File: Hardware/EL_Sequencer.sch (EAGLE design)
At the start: 109 parts, among them J1 Battery, J2 DC-OUTPUT, J3 AC-INPUT, U1 LM317, U10 Z0103MN, U11 Z0103MN, U12 Z0103MN, U13 MOC3063S, U14 MOC3063S, U15 MOC3063S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

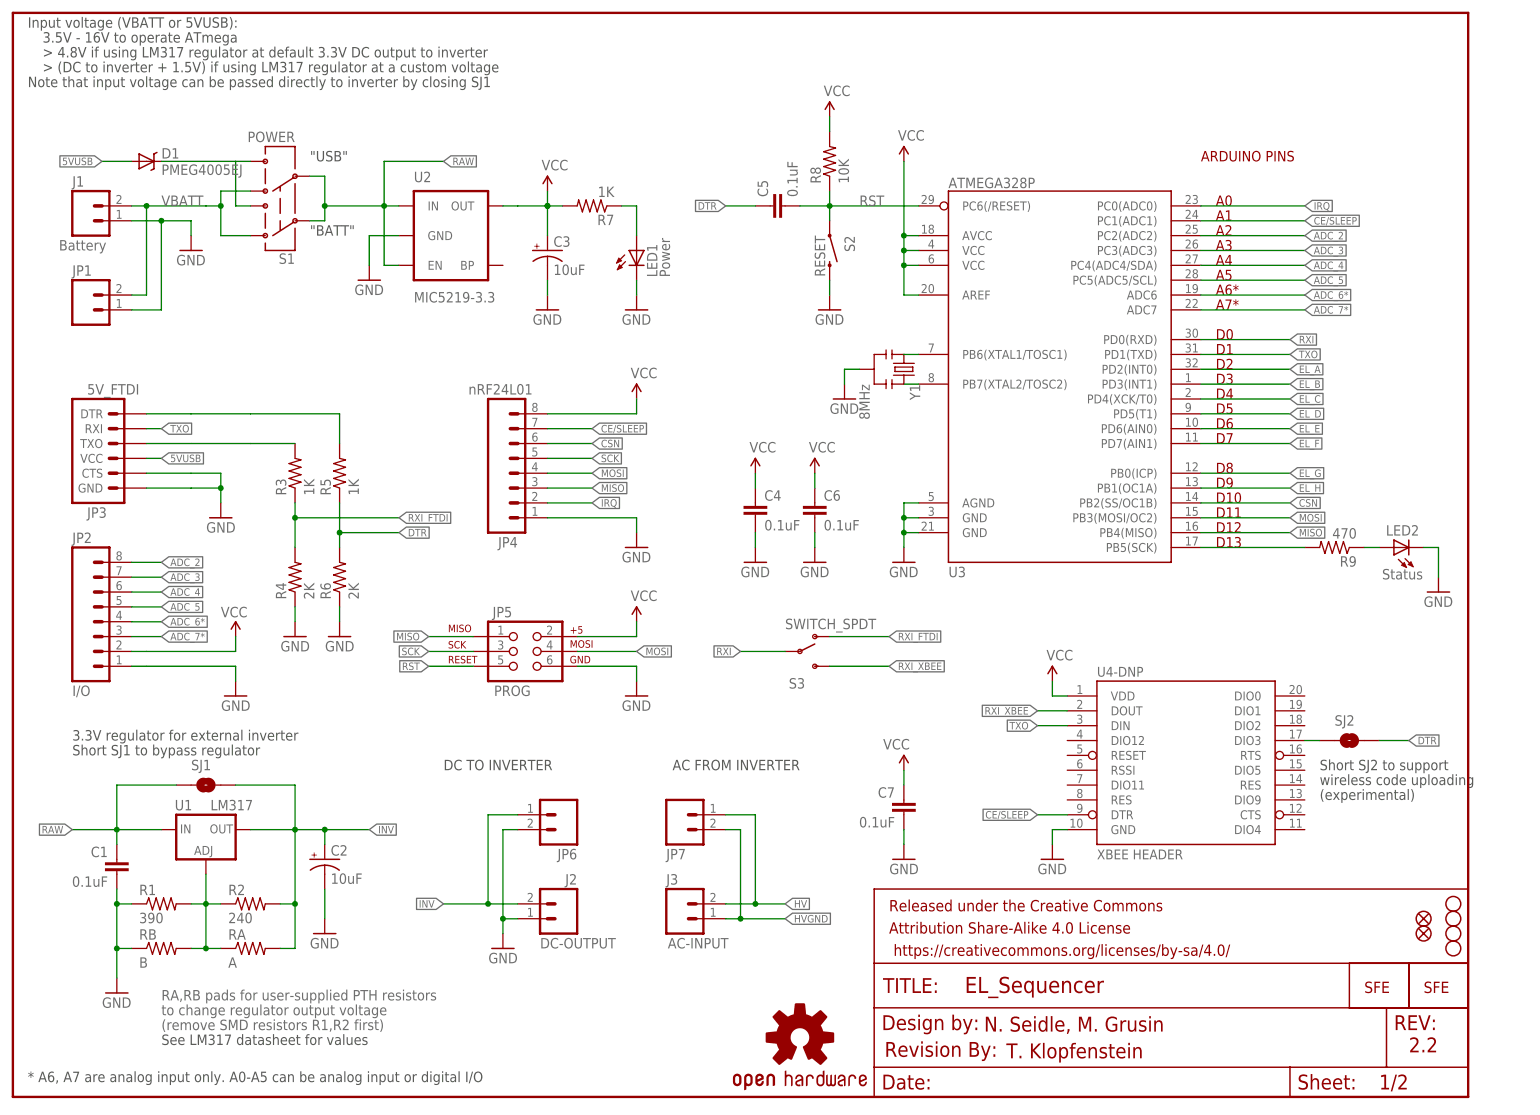
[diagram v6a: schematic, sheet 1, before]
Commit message: Updates to V2.3
> Swapped LED resistors LED1 (green) now has 470, LED2 (red) now has 1K
> Added heatsink pours for 3.3V reg U2
> Reworked FTDI/XBEE switch, throw is now in direction of respective
connectors, swapped silk, added silk to bottom
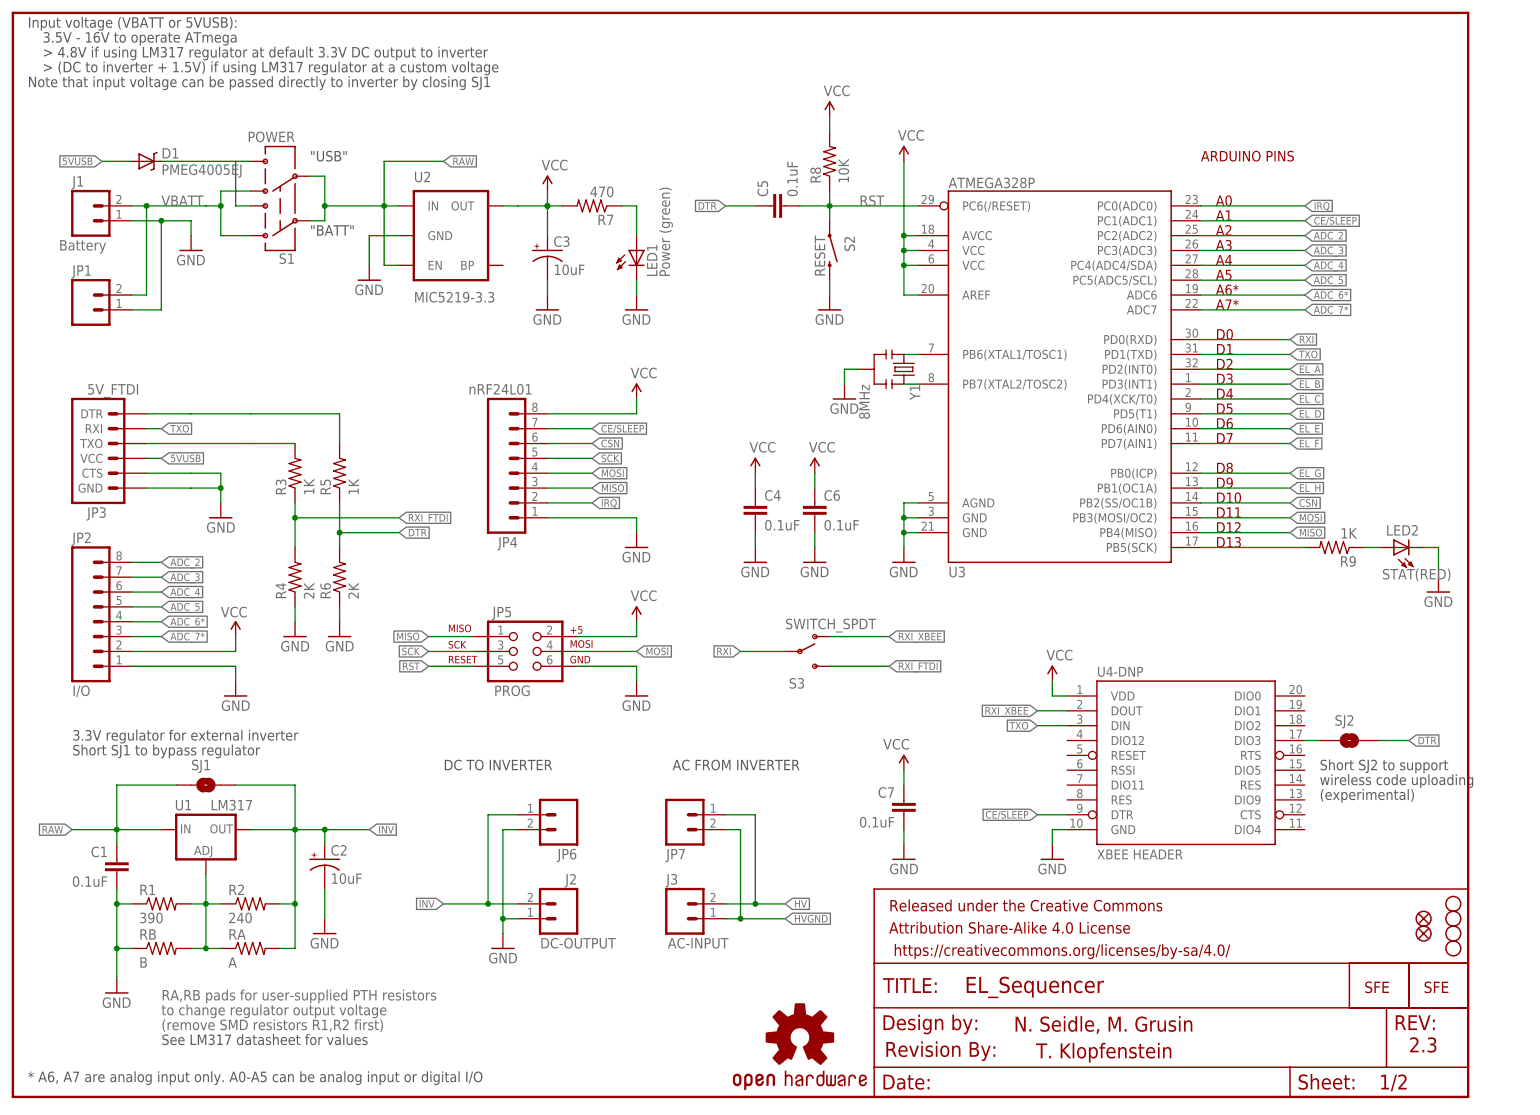
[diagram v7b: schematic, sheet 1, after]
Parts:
- LED1: value Power -> Power (green)
- LED2: value Status -> STAT(RED)
- R7: value 1K -> 470
- R9: value 470 -> 1K
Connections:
- net RXI_FTDI: now also S3.S; no longer S3.O
- net RXI_XBEE: now also S3.O; no longer S3.S
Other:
- note added: "2.3"
- note removed: "2.2"
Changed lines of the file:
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@@
 <part name="C6" library="SparkFun-Capacitors" deviceset="0.1UF-25V(+80/-20%)(0603)" device="" value="0.1uF"/>
 <part name="GND11" library="supply1" deviceset="GND" device=""/>
-<part name="R7" library="SparkFun-Resistors" deviceset="1KOHM1/10W1%(0603)" device="" value="1K"/>
-<part name="LED1" library="SparkFun" deviceset="LED" device="0603" value="Power"/>
+<part name="R7" library="SparkFun-Resistors" deviceset="1KOHM1/10W1%(0603)" device="" value="470"/>
+<part name="LED1" library="SparkFun" deviceset="LED" device="0603" value="Power (green)"/>
 <part name="GND9" library="SparkFun" deviceset="GND" device=""/>
 <part name="C3" library="SparkFun-Capacitors" deviceset="10UF-16V-10%(TANT)" device="" value="10uF"/>
@@
 <part name="U$5" library="SparkFun" deviceset="STAND-OFF" device=""/>
 <part name="U3" library="SparkFun" deviceset="ATMEGA168" device="" value="ATMEGA328P"/>
-<part name="LED2" library="SparkFun" deviceset="LED" device="0603" value="Status"/>
-<part name="R9" library="SparkFun-Resistors" deviceset="1KOHM1/10W1%(0603)" device="" value="470"/>
+<part name="LED2" library="SparkFun" deviceset="LED" device="0603" value="STAT(RED)"/>
+<part name="R9" library="SparkFun-Resistors" deviceset="1KOHM1/10W1%(0603)" device="" value="1K"/>
 <part name="GND14" library="SparkFun" deviceset="GND" device=""/>
 <part name="GND15" library="SparkFun" deviceset="GND" device=""/>
@@
 <text x="205.74" y="96.52" size="1.778" layer="94">D12</text>
 <text x="205.74" y="93.98" size="1.778" layer="94">D13</text>
-<text x="166.116" y="11.176" size="2.54" layer="94">N. Seidle, M. Grusin</text>
-<text x="238.76" y="7.62" size="2.54" layer="94">2.2</text>
+<text x="171.196" y="11.176" size="2.54" layer="94">N. Seidle, M. Grusin</text>
+<text x="238.76" y="7.62" size="2.54" layer="94">2.3</text>
 <text x="10.16" y="58.42" size="1.778" layer="97">Short SJ1 to bypass regulator</text>
 <text x="10.16" y="60.96" size="1.778" layer="97">3.3V regulator for external inverter</text>
@@
 <text x="50.8" y="160.02" size="1.778" layer="97">"USB"</text>
 <text x="50.8" y="147.32" size="1.778" layer="97">"BATT"</text>
-<text x="169.926" y="6.604" size="2.54" layer="94">T. Klopfenstein</text>
+<text x="175.006" y="6.604" size="2.54" layer="94">T. Klopfenstein</text>
 </plain>
 <instances>
@@
 <net name="RXI_FTDI" class="0">
 <segment>
-<pinref part="S3" gate="G$1" pin="O"/>
-<wire x1="139.7" y1="78.74" x2="149.86" y2="78.74" width="0.2032" layer="91"/>
-<label x="149.86" y="78.74" size="1.27" layer="95" xref="yes"/>
+<label x="149.86" y="73.66" size="1.27" layer="95" xref="yes"/>
+<wire x1="139.7" y1="73.66" x2="149.86" y2="73.66" width="0.2032" layer="91"/>
+<pinref part="S3" gate="G$1" pin="S"/>
 </segment>
 <segment>
@@
 <net name="RXI_XBEE" class="0">
 <segment>
-<pinref part="S3" gate="G$1" pin="S"/>
-<wire x1="139.7" y1="73.66" x2="149.86" y2="73.66" width="0.2032" layer="91"/>
-<label x="149.86" y="73.66" size="1.27" layer="95" xref="yes"/>
-</segment>
-<segment>
+<label x="149.86" y="78.74" size="1.27" layer="95" xref="yes"/>
+<wire x1="139.7" y1="78.74" x2="149.86" y2="78.74" width="0.2032" layer="91"/>
+<pinref part="S3" gate="G$1" pin="O"/>
+</segment>
+<segment>

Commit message: Updating parts to proper libraries, swapped stat LED to blue
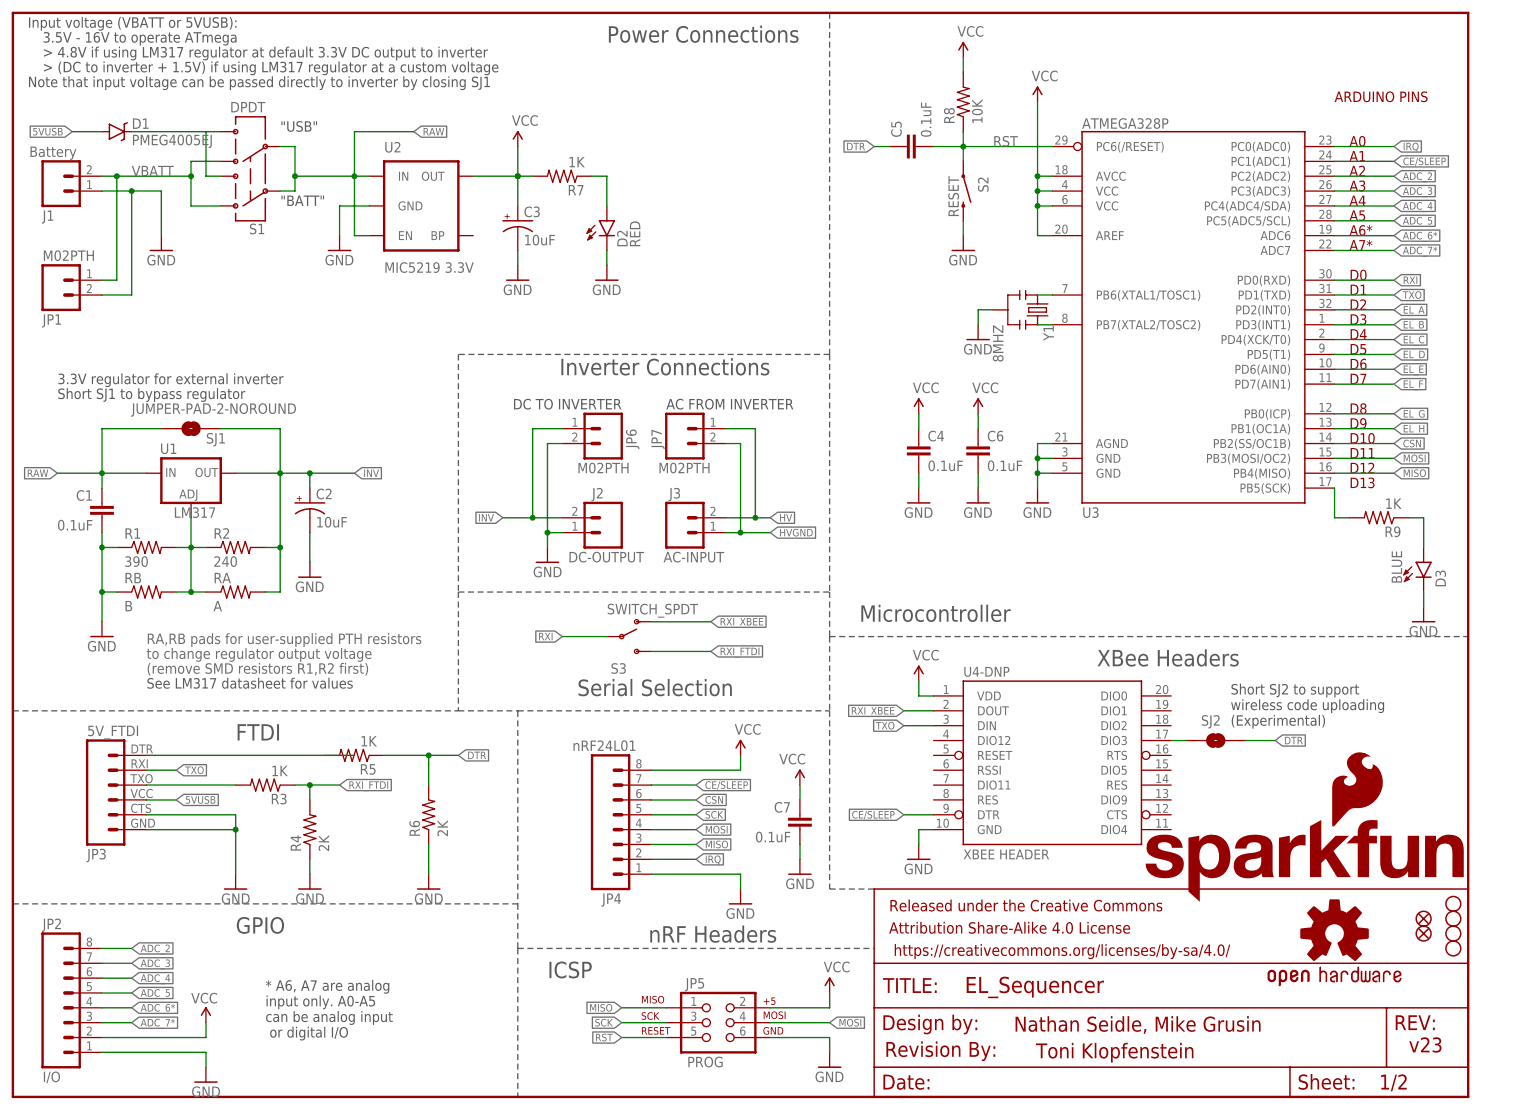
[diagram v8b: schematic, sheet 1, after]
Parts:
- removed LED1: Power (green), SparkFun:LED0603
- removed LED2: STAT(RED), SparkFun:LED0603
- added D2: RED, SparkFun-LED:LED-RED0603
- added D3: BLUE, SparkFun-LED:LED-BLUE0603
- J1, J2, J3: device SparkFun:M02-JST-2MM-SMT -> SparkFun-Connectors:M02-JST-2MM-SMT
- J10, J11, J4, J5, J6, J7, J8, J9: value (none) -> M02-JST-2MM-SMT; device SparkFun:M02-JST-2MM-SMT -> SparkFun-Connectors:M02-JST-2MM-SMT
- JP1, JP10, JP11, JP12, JP13, JP14, JP15, JP16, JP6, JP7, JP9: value (none) -> M02PTH; device SparkFun:M02PTH -> SparkFun-Connectors:M02PTH
- JP2: device mike-temp:M08_ROUND -> SparkFun-Connectors:M08
- JP3: device SparkFun:ARDUINO_SERIAL_PROGRAMPTH -> SparkFun-Connectors:FTDI_BASICPTH
- JP4: device SparkFun:M081X08 -> SparkFun-Connectors:M08SILK_FEMALE_PTH
- JP5: device SparkFun:AVR_SPI_PRG_6PTH -> SparkFun-Connectors:AVR_SPI_PRG_6PTH
- JP8: value LOGO-SFESK -> SFE_LOGO_FLAME.2_INCH; device SparkFun-Aesthetics:LOGO-SFESK -> SparkFun-Aesthetics:SFE_LOGO_FLAME.2_INCH
- R3, R5, R9: device SparkFun-Resistors:1KOHM1/10W1%(0603) -> SparkFun-Resistors:1KOHM-1/10W-1%(0603)
- R7: value 470 -> 1K; device SparkFun-Resistors:1KOHM1/10W1%(0603) -> SparkFun-Resistors:1KOHM-1/10W-1%(0603)
- R8: device SparkFun-Resistors:10KOHM1/10W1%(0603)0603 -> SparkFun-Resistors:10KOHM-1/10W-1%(0603)0603
- RA, RB: device SparkFun:RESISTORPTH-1/4W -> SparkFun-Resistors:RESISTORPTH-1/4W
- S1: value POWER -> DPDT; device SparkFun:SWITCH-DPDTSMD -> SparkFun-Electromechanical:SWITCH-DPDTAYZ0202
- S2: device SparkFun:SWITCH-MOMENTARY-2SMD -> SparkFun-Electromechanical:SWITCH-MOMENTARY-2SMD
- SJ1: value SOLDERJUMPERROUND -> JUMPER-PAD-2-NOROUND; device mike-temp:SOLDERJUMPERROUND -> SparkFun-Passives:JUMPER-PAD-2-NOROUND
- SJ2: value SOLDERJUMPERNO -> JUMPER-PAD-2-NOYES_SILK; device SparkFun-Passives:SOLDERJUMPERNO -> SparkFun-Passives:JUMPER-PAD-2-NOYES_SILK
- U$1: value OSHW-LOGOS -> OSHW-LOGOM; device SparkFun-Aesthetics:OSHW-LOGOS -> SparkFun-Aesthetics:OSHW-LOGOM
- U$2: value LOGO-SFENEW -> SFE_LOGO_NAME_FLAME.2_INCH; device SparkFun:LOGO-SFENEW -> SparkFun-Aesthetics:SFE_LOGO_NAME_FLAME.2_INCH
- U$5, U$6, U$7, U$8: device SparkFun:STAND-OFF -> SparkFun-Electromechanical:STAND-OFF
- U1: device SparkFun:V_REG_317DPACK -> SparkFun-PowerIC:V_REG_317DPACK
- U10, U11, U12, U17, U18, U19, U20, U9: device mike-temp:TRIACSMD -> SparkFun-DiscreteSemi:TRIAC-HPSMD
- U13, U14, U15, U16, U5, U6, U7, U8: device mike-temp:MOC3063S -> SparkFun-DiscreteSemi:MOC3063S
- U2: value MIC5219-3.3 -> MIC5219 3.3V; device SparkFun:V_REG_LDOSMD -> SparkFun-PowerIC:V_REG_MIC52193.3V
- U3: device SparkFun:ATMEGA168 -> SparkFun-DigitalIC:ATMEGA328_SMT
- U4-DNP: device mike-temp:XBEE-1LONGPAD -> SparkFun-RF:XBEE-1LONGPAD
- Y1: value 8MHz -> 8MHZ; device SparkFun:RESONATORSMD -> SparkFun-FreqCtrl:RESONATOR8MHZ
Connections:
- net 5VUSB: now also JP3.4; no longer JP3.VCC
- net FTDI_DTR: now also JP3.1; no longer JP3.DTR
- net FTDI_RXI: now also JP3.3; no longer JP3.TXO
- net GND: now also D2.C, D3.C, J1.2, J2.2, JP1.2, JP3.5, JP3.6; no longer J1.1, J2.1, JP1.1, JP3.CTS, JP3.GND, LED1.C, LED2.C
- net HV: now also J3.1; no longer J3.2
- net HVGND: now also J10.2, J11.2, J3.2, J4.2, J5.2, J6.2, J7.2, J8.2, J9.2; no longer J10.1, J11.1, J3.1, J4.1, J5.1, J6.1, J7.1, J8.1, J9.1
- net INV: now also J2.1; no longer J2.2
- net N$14: now also D3.A; no longer LED2.A
- net N$16: now also J6.1; no longer J6.2
- net N$20: now also J7.1; no longer J7.2
- net N$21: now also J4.1; no longer J4.2
- net N$25: now also J8.1; no longer J8.2
- net N$29: now also J9.1; no longer J9.2
- net N$33: now also J10.1; no longer J10.2
- net N$37: now also J11.1; no longer J11.2
- net N$4: now also D2.A; no longer LED1.A
- net N$9: now also J5.1; no longer J5.2
- net TXO: now also JP3.2; no longer JP3.RXI
- net VBATT: now also J1.1, JP1.1; no longer J1.2, JP1.2
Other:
- note added: "EL Channels"
- note added: "FTDI"
- note added: "GPIO"
- note added: "ICSP"
- note added: "Inverter Connections"
- note added: "Microcontroller"
- note added: "Nathan Seidle, Mike Grusin"
- note added: "Power Connections"
- note added: "Revision by: Toni Klopfenstein"
- note added: "Serial Selection"
- note added: "Short SJ2 to support wireless code uploading (Experimental)"
- note added: "Toni Klopfenstein"
- note added: "XBee Headers"
- note added: "nRF Headers"
- note added: "v23"
- note removed: "(experimental)"
- note removed: "2.1"
- note removed: "2.3"
- note removed: "Short SJ2 to support"
- note removed: "T. Klopfenstein"
- note removed: "wireless code uploading"
- moved on the sheet: C1, C2, C3, C4, C5, C6, C7, J1, J10, J11, J2, J3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
